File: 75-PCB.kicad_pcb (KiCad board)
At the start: 2 copper layers, 315.1 x 125.4 mm, 324 parts, among them J1 AVR-ISP-6, Q1 2N7002, SW1 SW_Push, U1 AT90USB1286-AU, U2 PRTR5V0U2X, Y1 16MHz

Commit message: Reset traces, changed component placement
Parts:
- removed R12: 500, Resistor_SMD:R_0805_2012Metric
- R4: value 1K -> 10K
- moved LED7 276.1 mm to (261.9, -231.0), turned to 270 degrees
- moved LED6 209.8 mm to (202.4, -231.0), turned to 270 degrees
- moved LED4 129.4 mm to (73.0, -231.0), turned to 270 degrees
- moved LED5 128.6 mm to (133.3, -231.0)
- moved LED3 122.2 mm to (11.1, -231.0)
- moved LED2 84.6 mm to (-4.76, -197.6), turned to 180 degrees
- moved LED1 73.2 mm to (-4.76, -159.5), turned to 0 degrees
- moved R1 66.1 mm to (283.4, -221.5), turned to 180 degrees
- moved R3 59.2 mm to (283.4, -208.8), turned to 180 degrees
- moved R2 56.2 mm to (283.4, -211.9), turned to 180 degrees
- moved R5 52.4 mm to (287.3, -151.0), turned to 270 degrees
- moved R4 45.7 mm to (272.3, -179.4), turned to 180 degrees
- moved Q1 21.7 mm to (296.1, -158.0)
- moved R10 20.7 mm to (290.5, -158.0)
- moved R11 19.3 mm to (292.9, -158.0), turned to 90 degrees
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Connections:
- LED2 pad 2: Net-(LED2-Pad2) -> Net-(LED1-Pad4)
- LED3 pad 2: Net-(LED3-Pad2) -> Net-(LED2-Pad4)
- LED4 pad 2: Net-(LED4-Pad2) -> Net-(LED3-Pad4)
- LED5 pad 2: Net-(LED5-Pad2) -> Net-(LED4-Pad4)
- LED6 pad 2: Net-(LED3-Pad4) -> Net-(LED5-Pad4)
- LED6 pad 4: Net-(LED5-Pad2) -> Net-(LED6-Pad4)
- LED7 pad 2: Net-(LED7-Pad2) -> Net-(LED6-Pad4)
- LED8 pad 2: Net-(LED5-Pad4) -> Net-(LED7-Pad4)
- LED8 pad 4: Net-(LED7-Pad2) -> Net-(LED8-Pad4)
- LED9 pad 2: Net-(LED7-Pad4) -> Net-(LED8-Pad4)
- LED9 pad 4: Net-(LED9-Pad4) -> RGBLED
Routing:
- net LEDGND: track 1695.9 -> 0.00 mm
- net ROW4: track 299.5 -> 0.00 mm
- net ROW5: track 288.8 -> 0.00 mm
- net ROW1: track 266.7 -> 0.00 mm
- net ROW0: track 266.7 -> 0.00 mm
- net ROW2: track 236.5 -> 0.00 mm
- net ROW3: track 215.9 -> 0.00 mm
- net COL6: track 131.1 -> 0.00 mm
- net COL11: track 119.7 -> 0.00 mm
- net COL10: track 118.2 -> 0.00 mm
- net COL9: track 118.2 -> 0.00 mm
- net COL2: track 112.5 -> 0.00 mm
- net COL14: track 111.2 -> 0.00 mm
- net COL1: track 110.5 -> 0.00 mm
- net COL4: track 110.2 -> 0.00 mm
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
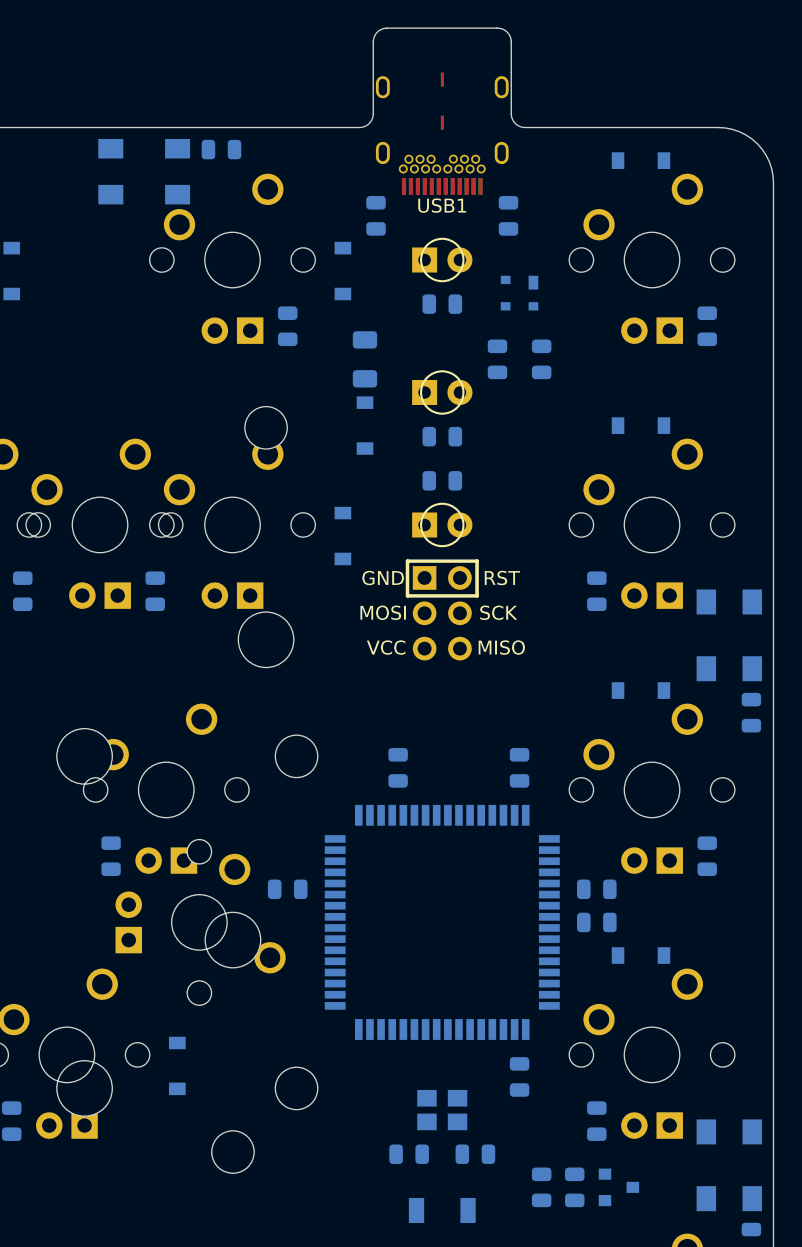
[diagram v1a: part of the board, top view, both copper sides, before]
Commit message: Finished USB and 5V traces
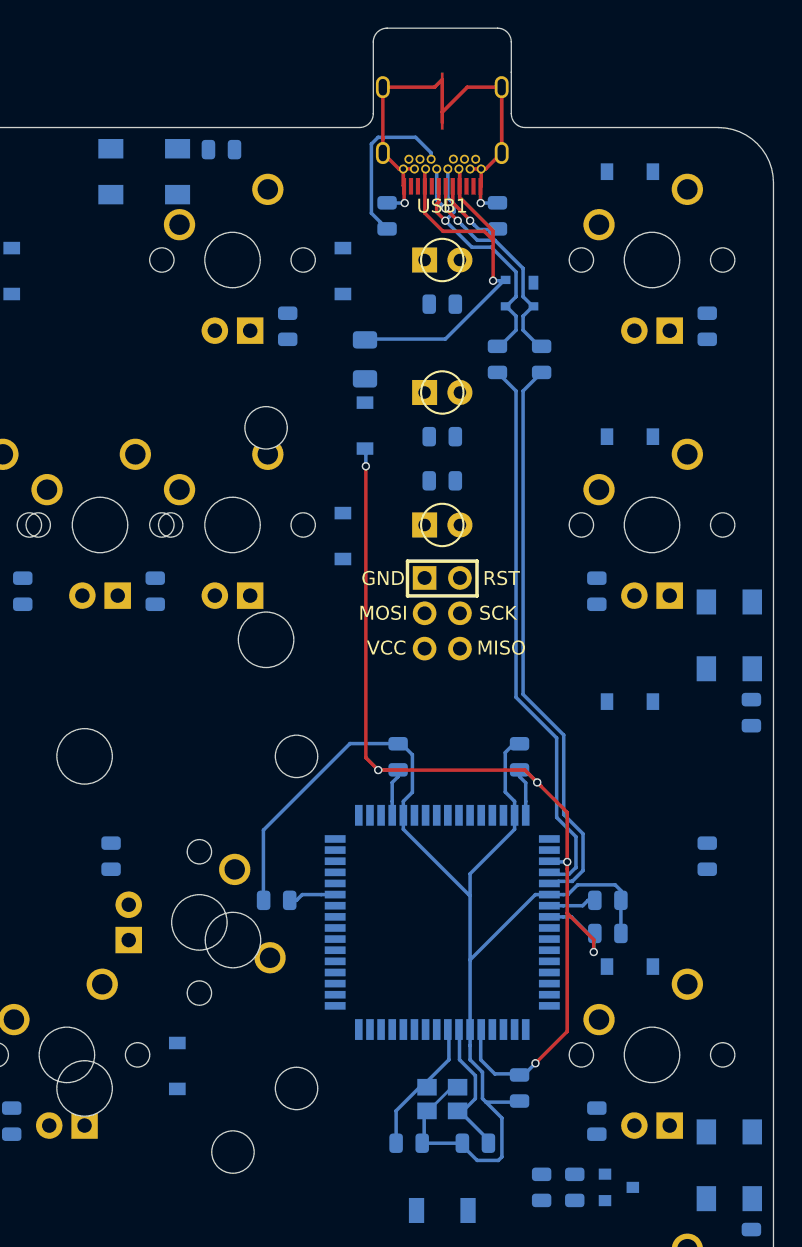
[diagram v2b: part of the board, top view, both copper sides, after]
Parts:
- removed MX_PGUP1: MX-LED, MX_Only:MXOnly-1U
- removed MX_\1: MX-LED, MX_Only:MXOnly-1.5U
- moved C3 8.77 mm to (280.2, -188.9)
- moved C4 8.77 mm to (288.9, -188.9)
- moved R4 1.12 mm to (271.5, -178.6)
- moved D83 1.12 mm to (296.9, -231.0)
- moved D85 1.12 mm to (296.9, -192.9)
- moved C5 1.12 mm to (295.3, -176.2)
- moved C7 1.12 mm to (295.3, -178.6)
- moved D84 1.12 mm to (296.9, -211.9)
- moved D89 1.12 mm to (296.9, -173.8)
- moved R6 0.79 mm to (287.3, -227.8)
- moved C6 0.79 mm to (288.9, -165.1)
- moved Y1 0.79 mm to (283.4, -164.3)
- moved C1 0.79 mm to (281.0, -161.1)
- moved C2 0.79 mm to (285.8, -161.1)
- moved R7 0.79 mm to (279.4, -227.8)
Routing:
- net GND: track 0.00 -> 129.8 mm, vias 0 -> 2
- net +5V: track 0.00 -> 84.3 mm, vias 0 -> 6
- net D+: track 0.00 -> 41.0 mm
- net D-: track 0.00 -> 40.1 mm
- net VCC: track 0.00 -> 30.8 mm, vias 0 -> 1
- net Net-(R8-Pad2): track 0.00 -> 20.2 mm, vias 0 -> 1
- net Net-(R9-Pad2): track 0.00 -> 19.0 mm, vias 0 -> 2
- net Net-(R7-Pad2): track 0.00 -> 12.0 mm
- net Net-(C2-Pad1): track 0.00 -> 10.4 mm
- net Net-(C1-Pad1): track 0.00 -> 10.1 mm
- net Net-(R6-Pad2): track 0.00 -> 5.24 mm, vias 0 -> 1
- net Net-(R4-Pad1): track 0.00 -> 3.44 mm
- net Net-(C7-Pad1): track 0.00 -> 3.43 mm

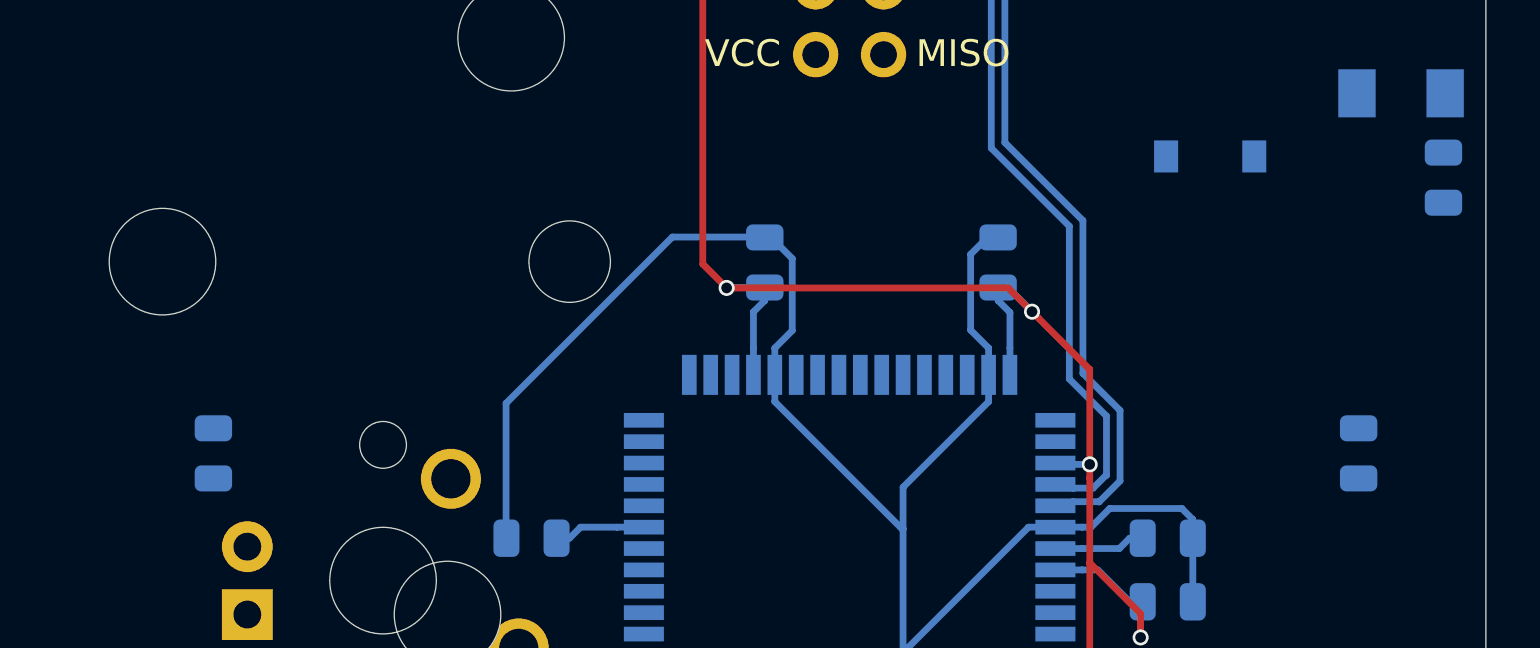
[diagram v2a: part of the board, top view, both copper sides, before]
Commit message: Fixed underglow LED schematic and switch footprints
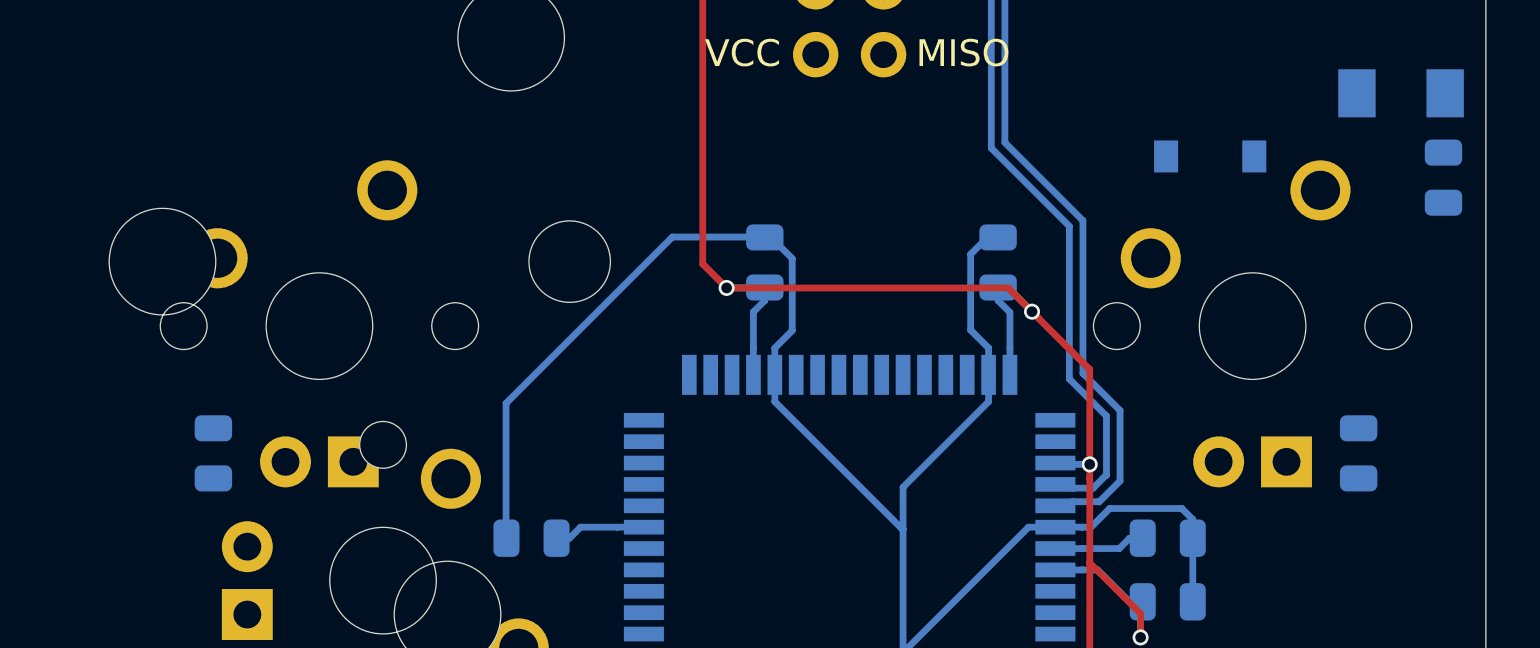
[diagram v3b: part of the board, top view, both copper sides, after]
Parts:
- added MX_PGUP1: MX-LED, MX_Only:MXOnly-1U, F.Cu at (298.4, -186.5)
- added MX_\1: MX-LED, MX_Only:MXOnly-1.5U, F.Cu at (263.5, -186.5)
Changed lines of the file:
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@@
     (tracks 263)
     (zones 0)
-    (modules 321)
+    (modules 323)
     (nets 288)
   )
@@
     (solder_mask_min_width 0.25)
     (aux_axis_origin 0 0)
-    (visible_elements 7FFFFFFF)
+    (visible_elements 7FFFF7FF)
     (pcbplotparams
       (layerselection 0x010fc_ffffffff)
@@
     (add_net VCC)
   )
+  (module MX_Only:MXOnly-1U (layer F.Cu)
+    (at 298.45 -186.53125)
+    (fp_text reference MX_PGUP1 (at 0 3.175) (layer Dwgs.User)
+      (effects (font (size 1 1) (thickness 0.15)))
+    )
+    (fp_text value MX-LED (at 0 -7.9375) (layer Dwgs.User)
+      (effects (font (size 1 1) (thickness 0.15)))
+    )
+    (fp_line (start -9.525 9.525) (end -9.525 -9.525) (layer Dwgs.User) (width 0.15))
+    (fp_line (start 9.525 9.525) (end -9.525 9.525) (layer Dwgs.User) (width 0.15))
+    (fp_line (start 9.525 -9.525) (end 9.525 9.525) (layer Dwgs.User) (width 0.15))
+    (fp_line (start -9.525 -9.525) (end 9.525 -9.525) (layer Dwgs.User) (width 0.15))
+    (fp_line (start -7 -7) (end -7 -5) (layer Dwgs.User) (width 0.15))
+    (fp_line (start -5 -7) (end -7 -7) (layer Dwgs.User) (width 0.15))
+    (fp_line (start -7 7) (end -5 7) (layer Dwgs.User) (width 0.15))
+    (fp_line (start -7 5) (end -7 7) (layer Dwgs.User) (width 0.15))
+    (fp_line (start 7 7) (end 7 5) (layer Dwgs.User) (width 0.15))
+    (fp_line (start 5 7) (end 7 7) (layer Dwgs.User) (width 0.15))
+    (fp_line (start 7 -7) (end 7 -5) (layer Dwgs.User) (width 0.15))
+    (fp_line (start 5 -7) (end 7 -7) (layer Dwgs.User) (width 0.15))
+    (pad "" np_thru_hole circle (at 5.08 0 48.0996) (size 1.75 1.75) (drill 1.75) (layers *.Cu *.Mask))
+    (pad "" np_thru_hole circle (at -5.08 0 48.0996) (size 1.75 1.75) (drill 1.75) (layers *.Cu *.Mask))
+    (pad 4 thru_hole rect (at 1.27 5.08) (size 1.905 1.905) (drill 1.04) (layers *.Cu B.Mask)
+      (net 196 "Net-(MX_PGUP1-Pad4)"))
+    (pad 3 thru_hole circle (at -1.27 5.08) (size 1.905 1.905) (drill 1.04) (layers *.Cu B.Mask)
+      (net 4 +5V))
+    (pad 1 thru_hole circle (at -3.81 -2.54) (size 2.25 2.25) (drill 1.47) (layers *.Cu B.Mask)
+      (net 158 COL15))
+    (pad "" np_thru_hole circle (at 0 0) (size 3.9878 3.9878) (drill 3.9878) (layers *.Cu *.Mask))
+    (pad 2 thru_hole circle (at 2.54 -5.08) (size 2.25 2.25) (drill 1.47) (layers *.Cu B.Mask)
+      (net 96 "Net-(D85-Pad2)"))
+  )
+  (module MX_Only:MXOnly-1.5U (layer F.Cu)
+    (at 263.525 -186.53125)
+    (fp_text reference MX_\1 (at 0 3.175) (layer Dwgs.User)
+      (effects (font (size 1 1) (thickness 0.15)))
+    )
+    (fp_text value MX-LED (at 0 -7.9375) (layer Dwgs.User)
+      (effects (font (size 1 1) (thickness 0.15)))
+    )
+    (fp_line (start -14.2875 9.525) (end -14.2875 -9.525) (layer Dwgs.User) (width 0.15))
+    (fp_line (start -14.2875 9.525) (end 14.2875 9.525) (layer Dwgs.User) (width 0.15))
+    (fp_line (start 14.2875 -9.525) (end 14.2875 9.525) (layer Dwgs.User) (width 0.15))
+    (fp_line (start -14.2875 -9.525) (end 14.2875 -9.525) (layer Dwgs.User) (width 0.15))
+    (fp_line (start -7 -7) (end -7 -5) (layer Dwgs.User) (width 0.15))
+    (fp_line (start -5 -7) (end -7 -7) (layer Dwgs.User) (width 0.15))
+    (fp_line (start -7 7) (end -5 7) (layer Dwgs.User) (width 0.15))
+    (fp_line (start -7 5) (end -7 7) (layer Dwgs.User) (width 0.15))
+    (fp_line (start 7 7) (end 7 5) (layer Dwgs.User) (width 0.15))
+    (fp_line (start 5 7) (end 7 7) (layer Dwgs.User) (width 0.15))
+    (fp_line (start 7 -7) (end 7 -5) (layer Dwgs.User) (width 0.15))
+    (fp_line (start 5 -7) (end 7 -7) (layer Dwgs.User) (width 0.15))
+    (pad "" np_thru_hole circle (at 5.08 0 48.0996) (size 1.75 1.75) (drill 1.75) (layers *.Cu *.Mask))
+    (pad "" np_thru_hole circle (at -5.08 0 48.0996) (size 1.75 1.75) (drill 1.75) (layers *.Cu *.Mask))
+    (pad 4 thru_hole rect (at 1.27 5.08) (size 1.905 1.905) (drill 1.04) (layers *.Cu B.Mask)
+      (net 144 "Net-(MX_\\1-Pad4)"))
+    (pad 3 thru_hole circle (at -1.27 5.08) (size 1.905 1.905) (drill 1.04) (layers *.Cu B.Mask)
+      (net 4 +5V))
+    (pad 1 thru_hole circle (at -3.81 -2.54) (size 2.25 2.25) (drill 1.47) (layers *.Cu B.Mask)
+      (net 145 COL13))
+    (pad "" np_thru_hole circle (at 0 0) (size 3.9878 3.9878) (drill 3.9878) (layers *.Cu *.Mask))
+    (pad 2 thru_hole circle (at 2.54 -5.08) (size 2.25 2.25) (drill 1.47) (layers *.Cu B.Mask)
+      (net 89 "Net-(D78-Pad2)"))
+  )
   (module Package_QFP:TQFP-64_14x14mm_P0.8mm (layer B.Cu)

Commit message: Finished row and LED ground traces
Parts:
- moved R48 0.79 mm to (130.2, -219.9)
- moved R50 0.79 mm to (130.2, -181.8)
- moved R53 0.79 mm to (165.9, -124.6)
- moved R57 0.79 mm to (154.0, -162.7)
- moved R58 0.79 mm to (144.5, -143.7)
- moved R59 0.79 mm to (168.3, -219.9)
- moved R61 0.79 mm to (168.3, -181.8)
- moved R64 0.79 mm to (201.6, -124.6)
- moved R65 0.79 mm to (192.1, -219.9)
- moved R66 0.79 mm to (177.8, -200.8)
- moved R68 0.79 mm to (192.1, -162.7)
- moved R70 0.79 mm to (215.9, -124.6)
- moved R75 0.79 mm to (201.6, -143.7)
- moved R78 0.79 mm to (215.9, -200.8)
- moved R79 0.79 mm to (225.4, -181.8)
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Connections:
- MX_LALT3 pad 4: Net-(MX_LALT1-Pad4) -> Net-(MX_LALT3-Pad4)
- MX_LWIN1 pad 4: Net-(MX_LWIN1-Pad4) -> Net-(MX_LALT3-Pad4)
- MX_LWIN2 pad 4: Net-(MX_LWIN1-Pad4) -> Net-(MX_LALT3-Pad4)
- R24 pad 1: Net-(MX_LWIN1-Pad4) -> Net-(MX_LALT3-Pad4)
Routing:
- net LEDGND: track 0.00 -> 1588.0 mm
- net ROW4: track 0.00 -> 299.5 mm
- net ROW5: track 0.00 -> 288.8 mm
- net ROW0: track 0.00 -> 266.7 mm
- net ROW1: track 0.00 -> 266.7 mm
- net ROW3: track 0.00 -> 253.1 mm, vias 0 -> 2
- net ROW2: track 0.00 -> 236.5 mm
- net Net-(D78-Pad2): track 0.00 -> 36.1 mm, vias 0 -> 1
- net Net-(D36-Pad2): track 0.00 -> 31.7 mm
- net Net-(MX_\1-Pad4): track 0.00 -> 30.8 mm, vias 0 -> 1
- net GND: track 129.8 -> 157.4 mm
- net Net-(D19-Pad2): track 0.00 -> 26.2 mm
- net Net-(MX_SPACE1-Pad4): track 0.00 -> 25.6 mm
- net Net-(D6-Pad2): track 0.00 -> 22.2 mm
- net Net-(D77-Pad2): track 0.00 -> 22.2 mm
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
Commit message: Finished column traces
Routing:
- net COL6: track 0.00 -> 130.1 mm
- net COL2: track 0.00 -> 129.1 mm
- net COL9: track 0.00 -> 124.4 mm
- net COL11: track 0.00 -> 119.7 mm
- net COL10: track 0.00 -> 119.6 mm
- net COL12: track 0.00 -> 116.9 mm
- net COL0: track 0.00 -> 116.9 mm
- net COL1: track 0.00 -> 110.5 mm
- net COL8: track 0.00 -> 110.1 mm
- net COL4: track 0.00 -> 110.0 mm
- net COL14: track 0.00 -> 106.1 mm
- net COL15: track 0.00 -> 103.6 mm
- net COL7: track 0.00 -> 90.1 mm
- net COL5: track 0.00 -> 90.1 mm
- net COL3: track 0.00 -> 88.0 mm
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
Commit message: Finished column and LED traces
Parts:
- removed MX_SPACE1: MX-LED, MX_Only:MXOnly-6.25U-ReversedStabilizers
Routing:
- net +5V: track 84.3 -> 1887.6 mm, vias 6 -> 16
- net Net-(MX_ENTER1-Pad4): track 6.84 -> 32.0 mm, vias 0 -> 2
- net COL14: track 106.1 -> 115.3 mm
- net COL1: track 110.5 -> 112.3 mm
- net COL5: track 90.1 -> 91.3 mm
- net COL13: track 85.7 -> 84.6 mm
- net COL10: track 119.6 -> 120.6 mm
- net COL9: track 124.4 -> 125.4 mm

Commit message: Finished LED matrix
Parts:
- added MX_SPACE1: MX-LED, MX_Only:MXOnly-6.25U-ReversedStabilizers, F.Cu at (123.0, -129.4)
- turned C13 to 270 degrees
- turned LED2 to 0 degrees
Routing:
- net +5V: track 1887.6 -> 2514.4 mm, vias 16 -> 24
- net LEDGND: track 1588.0 -> 1836.5 mm, vias 0 -> 13
- net GND: track 157.4 -> 245.9 mm, vias 2 -> 5
- net Net-(LED5-Pad4): track 0.00 -> 65.6 mm
- net Net-(LED3-Pad4): track 0.00 -> 58.5 mm
- net Net-(LED6-Pad4): track 0.00 -> 57.2 mm, vias 0 -> 2
- net Net-(LED4-Pad4): track 0.00 -> 56.9 mm
- net ROW2: track 236.5 -> 287.4 mm, vias 0 -> 4
- net ROW3: track 253.1 -> 301.4 mm, vias 2 -> 4
- net ROW0: track 266.7 -> 294.4 mm, vias 0 -> 2
- net ROW1: track 266.7 -> 292.5 mm, vias 0 -> 2
- net Net-(Q1-Pad1): track 0.00 -> 4.56 mm
- net Net-(MX_SPACE1-Pad4): track 25.6 -> 26.1 mm
